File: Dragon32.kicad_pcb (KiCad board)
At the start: 2 copper layers, 253 x 173.5 mm, 207 parts, among them IC1 HYB4116, IC10 LM318, IC11 MC14053, IC12 MC6847, IC13 74LS273, IC14 74HC86, IC15 MC6883, IC16 74HC244, IC19 MC6809E, IC2 HYB4116, IC20 MC14529B, IC21 74HC123, IC22 74HC00, IC23 74HC74, IC24 74HC244, IC25 LM393, IC26 MC6821, IC27 74HC20, IC28 74HC393, IC29 74HC393, IC3 HYB4116, IC30 74HC32, IC31 74HC02, IC32 74HC390, IC33 74HC138, IC34 74HC245, IC35 MC6821, IC39 28C256, IC4 HYB4116, IC40 74HC08, IC5 HYB4116, IC6 HYB4116, IC7 HYB4116, IC8 HYB4116, IC9 LM1889N, SW1 RESET, SW2 SW_DIP_x02

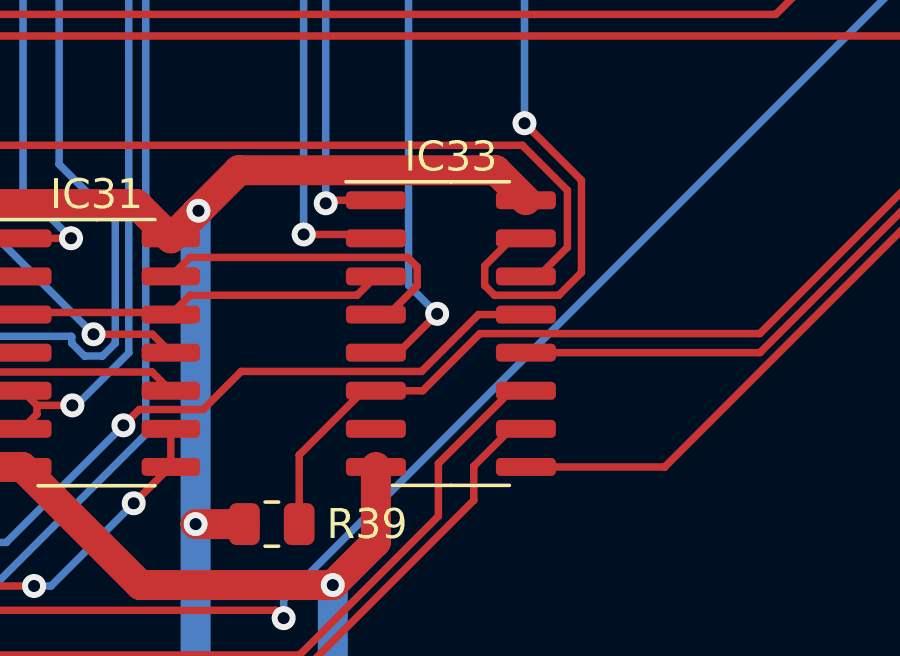
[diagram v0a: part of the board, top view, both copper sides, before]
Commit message: fix footprint of IC33
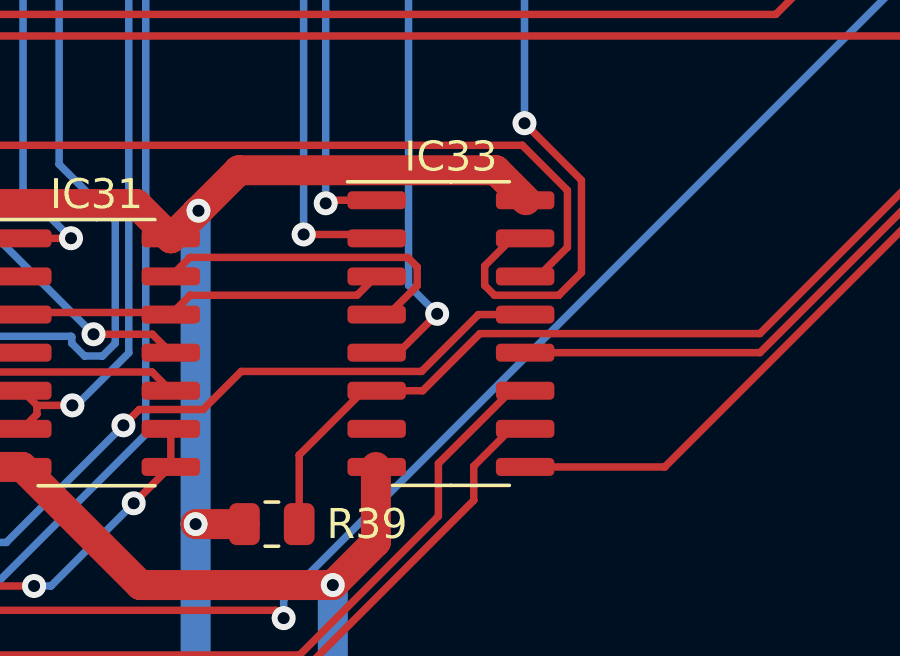
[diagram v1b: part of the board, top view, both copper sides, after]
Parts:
- IC33: footprint Package_SO:SOP-16_3.9x9.9mm_P1.27mm -> Package_SO:SOIC-16_3.9x9.9mm_P1.27mm
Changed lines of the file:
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@@
     )
   )
-  (footprint "Package_SO:SOP-16_3.9x9.9mm_P1.27mm" (layer "F.Cu")
+  (footprint "Package_SO:SOIC-16_3.9x9.9mm_P1.27mm" (layer "F.Cu")
     (at 250.698 142.748)
-    (descr "SOP, 16 Pin (https://www.diodes.com/assets/Datasheets/PAM8403.pdf), generated with kicad-footprint-generator ipc_gullwing_generator.py")
-    (tags "SOP SO")
+    (descr "SOIC, 16 Pin (JEDEC MS-012AC, https://www.analog.com/media/en/package-pcb-resources/package/pkg_pdf/soic_narrow-r/r_16.pdf), generated with kicad-footprint-generator ipc_gullwing_generator.py")
+    (tags "SOIC SO")
     (property "Sheetfile" "sam.kicad_sch")
     (property "Sheetname" "SAM")
@@
       (effects (font (size 0.98 0.98) (thickness 0.15)))
     )
-    (fp_line (start 0 -5.06) (end -3.5 -5.06) (layer "F.SilkS") (width 0.12))
     (fp_line (start 0 5.06) (end 1.95 5.06) (layer "F.SilkS") (width 0.12))
     (fp_line (start 0 -5.06) (end 1.95 -5.06) (layer "F.SilkS") (width 0.12))
+    (fp_line (start 0 -5.06) (end -3.45 -5.06) (layer "F.SilkS") (width 0.12))
     (fp_line (start 0 5.06) (end -1.95 5.06) (layer "F.SilkS") (width 0.12))
-    (fp_line (start -3.75 5.2) (end 3.75 5.2) (layer "F.CrtYd") (width 0.05))
-    (fp_line (start 3.75 5.2) (end 3.75 -5.2) (layer "F.CrtYd") (width 0.05))
-    (fp_line (start -3.75 -5.2) (end -3.75 5.2) (layer "F.CrtYd") (width 0.05))
-    (fp_line (start 3.75 -5.2) (end -3.75 -5.2) (layer "F.CrtYd") (width 0.05))
+    (fp_line (start -3.7 5.2) (end 3.7 5.2) (layer "F.CrtYd") (width 0.05))
+    (fp_line (start 3.7 5.2) (end 3.7 -5.2) (layer "F.CrtYd") (width 0.05))
+    (fp_line (start 3.7 -5.2) (end -3.7 -5.2) (layer "F.CrtYd") (width 0.05))
+    (fp_line (start -3.7 -5.2) (end -3.7 5.2) (layer "F.CrtYd") (width 0.05))
+    (fp_line (start -1.95 4.95) (end -1.95 -3.975) (layer "F.Fab") (width 0.1))
     (fp_line (start -1.95 -3.975) (end -0.975 -4.95) (layer "F.Fab") (width 0.1))
     (fp_line (start -0.975 -4.95) (end 1.95 -4.95) (layer "F.Fab") (width 0.1))
-    (fp_line (start -1.95 4.95) (end -1.95 -3.975) (layer "F.Fab") (width 0.1))
+    (fp_line (start 1.95 -4.95) (end 1.95 4.95) (layer "F.Fab") (width 0.1))
     (fp_line (start 1.95 4.95) (end -1.95 4.95) (layer "F.Fab") (width 0.1))
-    (fp_line (start 1.95 -4.95) (end 1.95 4.95) (layer "F.Fab") (width 0.1))
-    (pad "1" smd roundrect (at -2.5 -4.445) (size 2 0.6) (layers "F.Cu" "F.Paste" "F.Mask") (roundrect_rratio 0.25)
+    (pad "1" smd roundrect (at -2.475 -4.445) (size 1.95 0.6) (layers "F.Cu" "F.Paste" "F.Mask") (roundrect_rratio 0.25)
       (net 134 "S0") (pinfunction "A0") (pintype "input"))
-    (pad "2" smd roundrect (at -2.5 -3.175) (size 2 0.6) (layers "F.Cu" "F.Paste" "F.Mask") (roundrect_rratio 0.25)
+    (pad "2" smd roundrect (at -2.475 -3.175) (size 1.95 0.6) (layers "F.Cu" "F.Paste" "F.Mask") (roundrect_rratio 0.25)
       (net 133 "S1") (pinfunction "A1") (pintype "input"))
-    (pad "3" smd roundrect (at -2.5 -1.905) (size 2 0.6) (layers "F.Cu" "F.Paste" "F.Mask") (roundrect_rratio 0.25)
+    (pad "3" smd roundrect (at -2.475 -1.905) (size 1.95 0.6) (layers "F.Cu" "F.Paste" "F.Mask") (roundrect_rratio 0.25)
       (net 132 "S2") (pinfunction "A2") (pintype "input"))
-    (pad "4" smd roundrect (at -2.5 -0.635) (size 2 0.6) (layers "F.Cu" "F.Paste" "F.Mask") (roundrect_rratio 0.25)
+    (pad "4" smd roundrect (at -2.475 -0.635) (size 1.95 0.6) (layers "F.Cu" "F.Paste" "F.Mask") (roundrect_rratio 0.25)
       (net 226 "Net-(IC31-Pad13)") (pinfunction "E1") (pintype "input"))
-    (pad "5" smd roundrect (at -2.5 0.635) (size 2 0.6) (layers "F.Cu" "F.Paste" "F.Mask") (roundrect_rratio 0.25)
+    (pad "5" smd roundrect (at -2.475 0.635) (size 1.95 0.6) (layers "F.Cu" "F.Paste" "F.Mask") (roundrect_rratio 0.25)
       (net 221 "Net-(IC33-Pad5)") (pinfunction "E2") (pintype "input"))
-    (pad "6" smd roundrect (at -2.5 1.905) (size 2 0.6) (layers "F.Cu" "F.Paste" "F.Mask") (roundrect_rratio 0.25)
+    (pad "6" smd roundrect (at -2.475 1.905) (size 1.95 0.6) (layers "F.Cu" "F.Paste" "F.Mask") (roundrect_rratio 0.25)
       (net 239 "EXTMEN") (pinfunction "E3") (pintype "input"))
-    (pad "7" smd roundrect (at -2.5 3.175) (size 2 0.6) (layers "F.Cu" "F.Paste" "F.Mask") (roundrect_rratio 0.25)
+    (pad "7" smd roundrect (at -2.475 3.175) (size 1.95 0.6) (layers "F.Cu" "F.Paste" "F.Mask") (roundrect_rratio 0.25)
       (net 240 "unconnected-(IC33-Pad7)") (pinfunction "O7") (pintype "output+no_connect"))
-    (pad "8" smd roundrect (at -2.5 4.445) (size 2 0.6) (layers "F.Cu" "F.Paste" "F.Mask") (roundrect_rratio 0.25)
+    (pad "8" smd roundrect (at -2.475 4.445) (size 1.95 0.6) (layers "F.Cu" "F.Paste" "F.Mask") (roundrect_rratio 0.25)
       (net 1 "GND") (pinfunction "GND") (pintype "power_in"))
-    (pad "9" smd roundrect (at 2.5 4.445) (size 2 0.6) (layers "F.Cu" "F.Paste" "F.Mask") (roundrect_rratio 0.25)
+    (pad "9" smd roundrect (at 2.475 4.445) (size 1.95 0.6) (layers "F.Cu" "F.Paste" "F.Mask") (roundrect_rratio 0.25)
       (net 241 "P2") (pinfunction "O6") (pintype "output"))
-    (pad "10" smd roundrect (at 2.5 3.175) (size 2 0.6) (layers "F.Cu" "F.Paste" "F.Mask") (roundrect_rratio 0.25)
+    (pad "10" smd roundrect (at 2.475 3.175) (size 1.95 0.6) (layers "F.Cu" "F.Paste" "F.Mask") (roundrect_rratio 0.25)
       (net 242 "P1") (pinfunction "O5") (pintype "output"))
-    (pad "11" smd roundrect (at 2.5 1.905) (size 2 0.6) (layers "F.Cu" "F.Paste" "F.Mask") (roundrect_rratio 0.25)
+    (pad "11" smd roundrect (at 2.475 1.905) (size 1.95 0.6) (layers "F.Cu" "F.Paste" "F.Mask") (roundrect_rratio 0.25)
       (net 201 "P0") (pinfunction "O4") (pintype "output"))
-    (pad "12" smd roundrect (at 2.5 0.635) (size 2 0.6) (layers "F.Cu" "F.Paste" "F.Mask") (roundrect_rratio 0.25)
+    (pad "12" smd roundrect (at 2.475 0.635) (size 1.95 0.6) (layers "F.Cu" "F.Paste" "F.Mask") (roundrect_rratio 0.25)
       (net 243 "R2") (pinfunction "O3") (pintype "output"))
-    (pad "13" smd roundrect (at 2.5 -0.635) (size 2 0.6) (layers "F.Cu" "F.Paste" "F.Mask") (roundrect_rratio 0.25)
+    (pad "13" smd roundrect (at 2.475 -0.635) (size 1.95 0.6) (layers "F.Cu" "F.Paste" "F.Mask") (roundrect_rratio 0.25)
       (net 148 "~{E17}") (pinfunction "O2") (pintype "output"))
-    (pad "14" smd roundrect (at 2.5 -1.905) (size 2 0.6) (layers "F.Cu" "F.Paste" "F.Mask") (roundrect_rratio 0.25)
+    (pad "14" smd roundrect (at 2.475 -1.905) (size 1.95 0.6) (layers "F.Cu" "F.Paste" "F.Mask") (roundrect_rratio 0.25)
       (net 149 "~{E18}") (pinfunction "O1") (pintype "output"))
-    (pad "15" smd roundrect (at 2.5 -3.175) (size 2 0.6) (layers "F.Cu" "F.Paste" "F.Mask") (roundrect_rratio 0.25)
+    (pad "15" smd roundrect (at 2.475 -3.175) (size 1.95 0.6) (layers "F.Cu" "F.Paste" "F.Mask") (roundrect_rratio 0.25)
       (net 147 "D.Out") (pinfunction "O0") (pintype "output"))
-    (pad "16" smd roundrect (at 2.5 -4.445) (size 2 0.6) (layers "F.Cu" "F.Paste" "F.Mask") (roundrect_rratio 0.25)
+    (pad "16" smd roundrect (at 2.475 -4.445) (size 1.95 0.6) (layers "F.Cu" "F.Paste" "F.Mask") (roundrect_rratio 0.25)
       (net 7 "+5V") (pinfunction "VCC") (pintype "power_in"))
-    (model "${KICAD6_3DMODEL_DIR}/Package_SO.3dshapes/SOP-16_3.9x9.9mm_P1.27mm.wrl"
+    (model "${KICAD6_3DMODEL_DIR}/Package_SO.3dshapes/SOIC-16_3.9x9.9mm_P1.27mm.wrl"
       (offset (xyz 0 0 0))
       (scale (xyz 1 1 1))

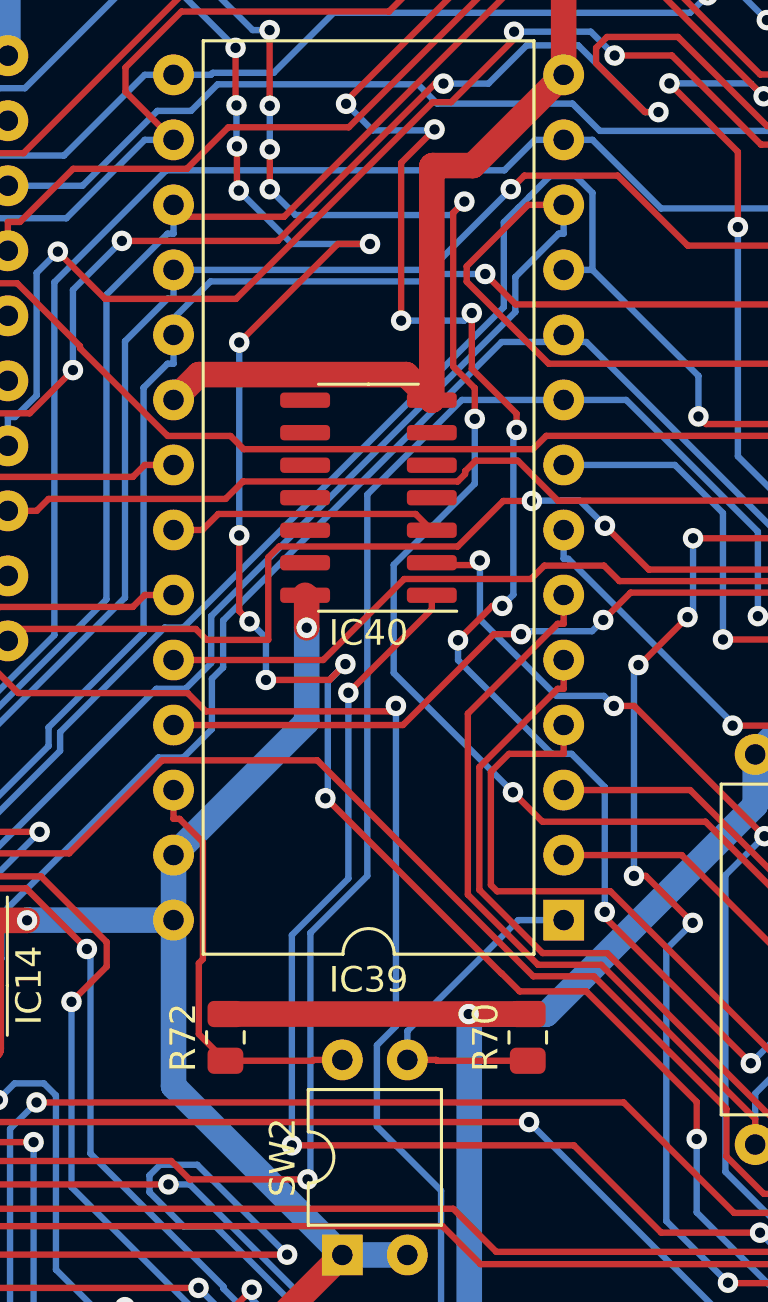
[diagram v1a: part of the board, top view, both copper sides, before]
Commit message: swap new and gate over to a single circuit chip
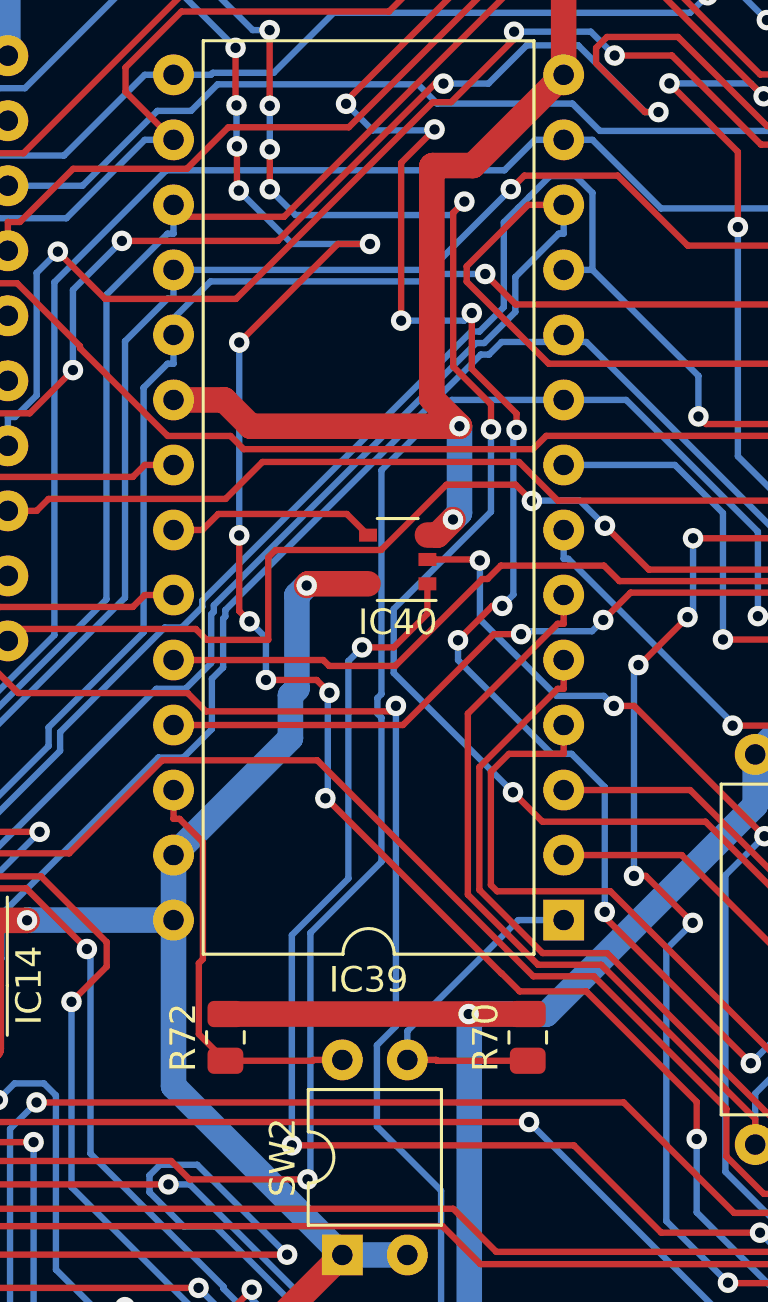
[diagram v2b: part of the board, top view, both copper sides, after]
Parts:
- IC40: value 74HC08 -> 74HC1G08; footprint Package_SO:SOIC-14_3.9x8.7mm_P1.27mm -> Package_SO:TSOP-5_1.65x3.05mm_P0.95mm
- moved IC40 2.67 mm to (189.6, 86.2)
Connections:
- IC40 pad 3: Net-(IC39-Pad22) -> GND
- IC40 pad 4: unconnected-(IC40-Pad4) -> Net-(IC39-Pad22)
- IC40 pad 5: unconnected-(IC40-Pad5) -> +5V
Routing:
- net GND: track 1963.4 -> 1970.6 mm, vias 56 -> 58
- net +5V: track 1650.7 -> 1653.4 mm
- net Net-(IC39-Pad22): track 10.6 -> 8.20 mm
- net Net-(IC31-Pad4): track 155.4 -> 153.4 mm
- net ~{E17}: track 117.2 -> 118.3 mm
- net ~{RAS0}: track 191.8 -> 192.3 mm
- net Z7: track 171.0 -> 171.6 mm

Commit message: convert memory to sram
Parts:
- removed C12, C14, C15, C16, C17, C18, C19, C20, C21, C50, C51, C52, C53, C54, C55, C56, C57, C58: 0.1uF, Capacitor_SMD:C_0805_2012Metric
- removed C13: 10uF, Capacitor_SMD:C_0805_2012Metric
- removed IC1, IC2, IC3, IC4, IC5, IC6, IC7, IC8: HYB4116, Package_DIP:DIP-16_W7.62mm
- removed JP1-2: 1 low, Connector_PinHeader_2.54mm:PinHeader_1x03_P2.54mm_Vertical
- removed JP3-4, JP5-6, JP7-8: 16k/32k, Connector_PinHeader_2.54mm:PinHeader_1x03_P2.54mm_Vertical
- removed R12: 22R, Resistor_SMD:R_0805_2012Metric
- added IC37: 74HC1G00, Package_SO:TSOP-5_1.65x3.05mm_P0.95mm, F.Cu at (211.5, 56.6)
- added IC38: 74HC574, Package_SO:SOIC-20W_7.5x12.8mm_P1.27mm, F.Cu at (222.5, 49.4)
- added IC41: UM61512, Package_DIP:DIP-32_W7.62mm, F.Cu at (233.8, 52.7)
- C10, C11: value 4.7uF -> 0.1uF
- IC16: footprint Package_DIP:DIP-20_W7.62mm -> Package_SO:SOIC-20W_7.5x12.8mm_P1.27mm
- JP13-14: value 16k/32k -> 32k/64k
- moved C11 34.0 mm to (233.8, 40.8), turned to -90 degrees
- moved C10 23.5 mm to (216.8, 41.1), turned to -90 degrees
- moved C27 12.0 mm to (119.0, 105.5), turned to -90 degrees
- moved R25 10.5 mm to (216.5, 60.3)
- moved R24 9.88 mm to (218.6, 60.3)
- moved IC16 9.72 mm to (263.7, 62.6)
- moved R23 9.30 mm to (220.6, 60.3)
- moved R22 8.80 mm to (222.6, 60.3)
- moved R20 8.40 mm to (224.7, 60.3)
- moved R19 8.10 mm to (226.7, 60.3)
- moved R21 7.92 mm to (228.7, 60.3)
- moved R69 3.30 mm to (193.5, 47.0)
- moved R10 2.16 mm to (193.5, 43.7)
- moved C5 0.13 mm to (129.8, 59.7)
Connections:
- C10 pad 1: RAM VBB -> GND
- C10 pad 2: GND -> +5V
- C11 pad 1: RAM VDD -> GND
- C11 pad 2: GND -> +5V
- IC31 pad 4: Net-(IC31-Pad4) -> (no net)
- IC31 pad 5: Z7 -> (no net)
- IC31 pad 6: Z7 -> (no net)
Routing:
- net GND: track 1970.6 -> 1773.5 mm, vias 58 -> 59
- net RAM VBB: track 186.2 -> 0.00 mm, vias 7 -> 0
- net RAM VDD: track 182.4 -> 0.00 mm, vias 3 -> 0
- net RAM VCC: track 154.2 -> 0.00 mm, vias 4 -> 0
- net Net-(IC31-Pad4): track 153.4 -> 0.00 mm, vias 18 -> 0
- net D7: track 303.0 -> 451.2 mm, vias 6 -> 5
- net Z0: track 134.4 -> 5.99 mm
- net Z5: track 134.4 -> 6.31 mm, vias 1 -> 0
- net Z6: track 133.5 -> 6.62 mm, vias 3 -> 0
- net Z1: track 131.2 -> 5.68 mm, vias 2 -> 0
- net Z4: track 128.9 -> 5.99 mm, vias 1 -> 0
- net DO0: track 253.7 -> 133.3 mm, vias 3 -> 2
- net Z2: track 122.8 -> 5.36 mm, vias 1 -> 0
- net Z3: track 121.3 -> 5.68 mm, vias 1 -> 0
- net Z7: track 171.6 -> 61.0 mm, vias 10 -> 1
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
